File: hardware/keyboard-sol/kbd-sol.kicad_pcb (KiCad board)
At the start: 2 copper layers, 396.2 x 117.7 mm, 186 parts, among them J1 Controller, SW10 TAB: 1.25x, SW11 I, SW12 2, SW13 Zero, SW14 Q, SW15 O, SW16 3, SW17 Dash, SW18 W, SW19 P, SW20 4, SW21 Caret, SW22 E, SW23 AT, SW24 5, SW25 LT Bracket, SW26 R, SW27 Return: 1.5x, SW28 6, SW29 Backslash, SW30 T, SW31 Line Feed, SW32 7, SW33 RT Bracket, SW34 Y, SW35 Load, SW36 LT Ctrl, SW37 J, SW38 Upper Case: 1.5x, SW39 M, SW4 ESC: 1.75x, SW40 Shift Lock: 1.5x, SW41 K, SW42 LT Shift: 1.5x, SW43 Comma, SW44 A, SW45 L, SW46 Z, SW47 Period, SW48 S, SW49 Semicolon, SW5 8, SW50 X, SW51 Slash, SW52 D, SW53 Colon, SW54 C, SW55 RT Shift: 2x, SW56 F, SW57 DEL, SW58 V, SW59 Mode Select: 1.75x, SW6 BREAK, SW60 G, SW61 Repeat: 1.25x, SW62 B, SW63 H, SW64 RT Ctrl, SW65 N, SW66 Local, SW67 NP Dash, SW68 NP 4, SW69 NP Zero, SW7 U, SW70 Up Arrow, SW71 NP 7, SW72 NP 1, SW73 NP period, SW74 LT Arrow, SW75 NP asterisk, SW76 NP 5, SW77 NP plus, SW78 Spacebar, SW79 NP 8, SW8 1, SW80 NP 2, SW81 RT Arrow, SW82 NP divide, SW83 NP 6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

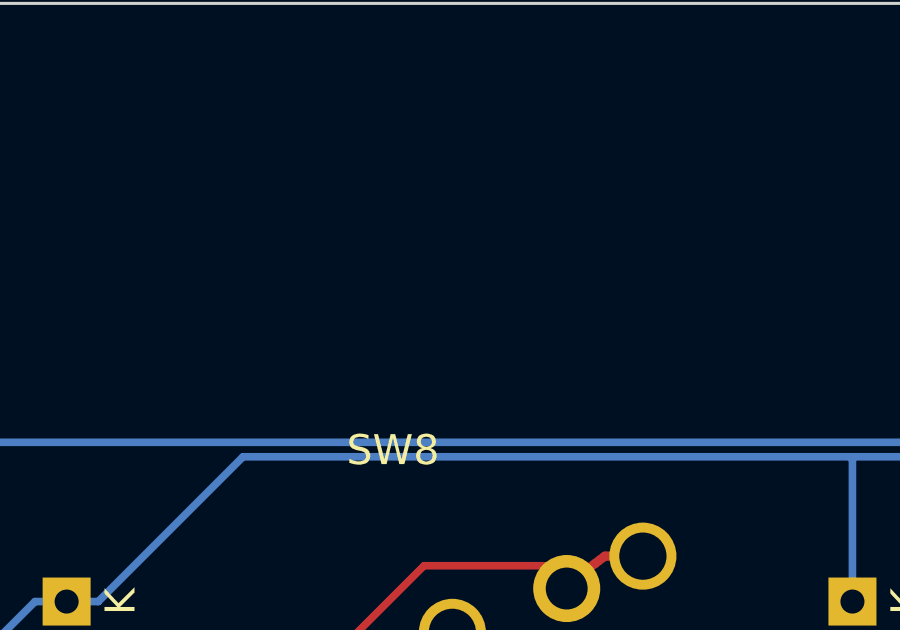
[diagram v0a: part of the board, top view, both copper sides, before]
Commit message: Add additional mounting holes to ASCII interface PCBS and Sol-20 PCB
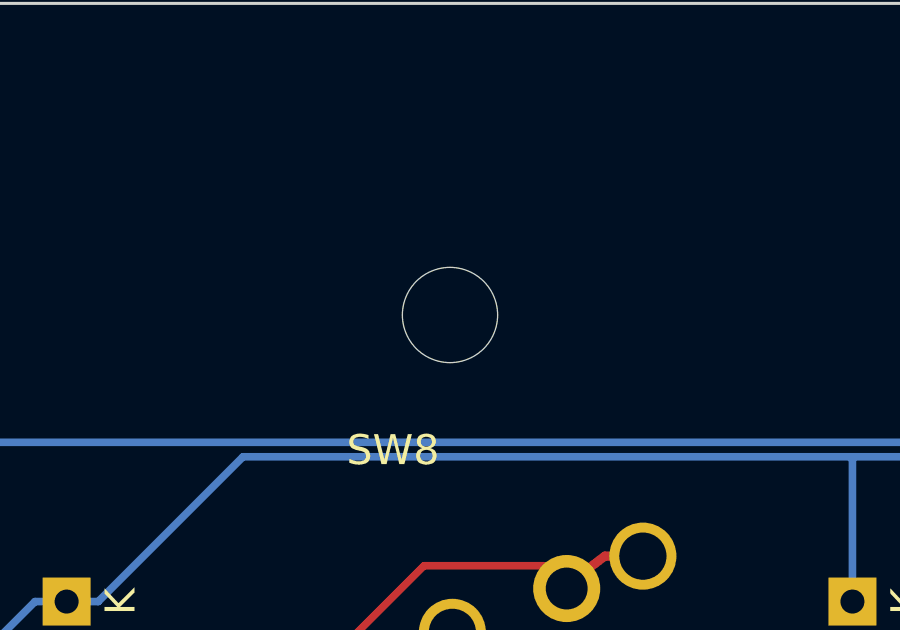
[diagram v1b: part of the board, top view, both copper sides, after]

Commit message: Add mounting holes for PCB along right side of keyboard
- moving interface PCB to right side eliminates clearance issues.
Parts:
- added REF**: MountingHole_3.2mm_M3, MountingHole:MountingHole_3.2mm_M3, F.Cu at (359.5, 114.1)
- added REF**: MountingHole_3.2mm_M3, MountingHole:MountingHole_3.2mm_M3, F.Cu at (392.7, 114.1)
- added REF**: MountingHole_3.2mm_M3, MountingHole:MountingHole_3.2mm_M3, F.Cu at (461.1, 114.1)
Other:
- board text added: "Interface MNT"
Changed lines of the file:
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@@
   (general
     (thickness 1.6)
-    (drawings 8)
+    (drawings 13)
     (tracks 1440)
     (zones 0)
-    (modules 186)
+    (modules 189)
     (nets 129)
   )
@@
     (add_net /Col0)
   )
+  (module MountingHole:MountingHole_3.2mm_M3 (layer F.Cu)
+    (at 359.5116 114.08156)
+    (descr "Mounting Hole 3.2mm, no annular, M3")
+    (tags "mounting hole 3.2mm no annular m3")
+    (attr virtual)
+    (fp_text reference REF** (at 0 -4.2) (layer F.SilkS) hide
+      (effects (font (size 1 1) (thickness 0.15)))
+    )
+    (fp_text value MountingHole_3.2mm_M3 (at 0 4.2) (layer F.Fab)
+      (effects (font (size 1 1) (thickness 0.15)))
+    )
+    (fp_circle (center 0 0) (end 3.45 0) (layer F.CrtYd) (width 0.05))
+    (fp_circle (center 0 0) (end 3.2 0) (layer Cmts.User) (width 0.15))
+    (fp_text user %R (at 0.3 0) (layer F.Fab)
+      (effects (font (size 1 1) (thickness 0.15)))
+    )
+    (pad 1 np_thru_hole circle (at 0 0) (size 3.2 3.2) (drill 3.2) (layers *.Cu *.Mask))
+  )
+  (module MountingHole:MountingHole_3.2mm_M3 (layer F.Cu)
+    (at 392.6586 114.08156)
+    (descr "Mounting Hole 3.2mm, no annular, M3")
+    (tags "mounting hole 3.2mm no annular m3")
+    (attr virtual)
+    (fp_text reference REF** (at 0 -4.2) (layer F.SilkS) hide
+      (effects (font (size 1 1) (thickness 0.15)))
+    )
+    (fp_text value MountingHole_3.2mm_M3 (at 0 4.2) (layer F.Fab)
+      (effects (font (size 1 1) (thickness 0.15)))
+    )
+    (fp_circle (center 0 0) (end 3.45 0) (layer F.CrtYd) (width 0.05))
+    (fp_circle (center 0 0) (end 3.2 0) (layer Cmts.User) (width 0.15))
+    (fp_text user %R (at 0.3 0) (layer F.Fab)
+      (effects (font (size 1 1) (thickness 0.15)))
+    )
+    (pad 1 np_thru_hole circle (at 0 0) (size 3.2 3.2) (drill 3.2) (layers *.Cu *.Mask))
+  )
+  (module MountingHole:MountingHole_3.2mm_M3 (layer F.Cu)
+    (at 461.1116 114.08156)
+    (descr "Mounting Hole 3.2mm, no annular, M3")
+    (tags "mounting hole 3.2mm no annular m3")
+    (attr virtual)
+    (fp_text reference REF** (at 0 -4.2) (layer F.SilkS) hide
+      (effects (font (size 1 1) (thickness 0.15)))
+    )
+    (fp_text value MountingHole_3.2mm_M3 (at 0 4.2) (layer F.Fab)
+      (effects (font (size 1 1) (thickness 0.15)))
+    )
+    (fp_text user %R (at 0.3 0) (layer F.Fab)
+      (effects (font (size 1 1) (thickness 0.15)))
+    )
+    (fp_circle (center 0 0) (end 3.2 0) (layer Cmts.User) (width 0.15))
+    (fp_circle (center 0 0) (end 3.45 0) (layer F.CrtYd) (width 0.05))
+    (pad 1 np_thru_hole circle (at 0 0) (size 3.2 3.2) (drill 3.2) (layers *.Cu *.Mask))
+  )
   (module unikbd:kbd_header_two_mounting_holes locked (layer F.Cu)
     (at 191.6938 208.9658 90)
@@
     )
   )
+  (gr_line (start 193.4464 117.2718) (end 237.6551 117.2718) (layer F.SilkS) (width 0.254))
+  (gr_text "Interface MNT" (at 214.8713 115.3541) (layer F.SilkS)
+    (effects (font (size 1.5 1.5) (thickness 0.3)))
+  )
+  (gr_text "Interface MNT" (at 459.7908 109.1565) (layer F.SilkS)
+    (effects (font (size 1.5 1.5) (thickness 0.3)))
+  )
+  (gr_line (start 363.2327 113.8174) (end 389.1407 113.8174) (layer F.SilkS) (width 0.254))
+  (gr_text "Interface MNT" (at 376.0343 112.3188) (layer F.SilkS)
+    (effects (font (size 1.5 1.5) (thickness 0.3)))
+  )
   (gr_text "SOL-20 keyboard rev 1.4" (at 362.7374 223.1644) (layer F.SilkS)

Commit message: Update Sol keyboard to 1.5 (Minor changes)
- Fix title in Schematic

- Slightly enlarge center post hole on switch footprint, to allow a bit of
tolerance. Very tight tolerance makes the keyboards hard to assemble.
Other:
- board text added: "SOL-20 keyboard rev 1.5"
- board text removed: "SOL-20 keyboard rev 1.4"

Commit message: Multiple fixes for keyboard PCB
- in combined CherryMX/futaba footprints, moved cherry pads down 1 mil and
futaba pads up 2 mil, to reduce risk of shortin of LED pads with futaba pad.
Adjusted all aligners accordingly

- Fixed centroid for combined diode footprint and adjusted PCB placement on
classic and SOL keyboards accordingly.

- Moved SMT pads in combined diode footprint to top layer, so pick & place file
will be usable.

- changes to futaba stabilizer design.  Longer post adapter passes through slots
in keyboard and aligner.

- Changed futaba post thickness gauge from board outline to a slot to improve
tolerance.

- Moved spacebar stabilizer bending guide to edge of PCB, in order to make it
more useful in bending PCBs.

- Changed Apple II mounting slots on classic keyboard from horizontal to
vertical orientation, to accommodate the different spacing offets due to the use
of spacers in angled mounting threads.
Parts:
- D1, D10, D11, D12, D13, D14, D15, D16, D17, D18, D19, D2, D20, D21, D22, D23, D24, D25, D26, D27, D28, D29, D3, D30, D31, D32, D33, D34, D35, D36, D37, D38, D39, D4, D40, D41, D42, D43, D44, D45, D46, D47, D48, D49, D5, D50, D51, D52, D53, D54, D55, D56, D57, D58, D59, D6, D60, D61, D62, D63, D64, D65, D66, D67, D68, D69, D7, D70, D71, D72, D73, D74, D75, D76, D77, D78, D79, D8, D80, D81, D82, D83, D84, D85, D9: footprint Diode_THT:D_DO-35_SOD27_P7.62mm_Horizontal -> unikbd:diode-combined
- moved D10 0.10 mm to (322.8, 127.0)
- moved D12 0.10 mm to (313.2, 146.1)
- moved D13 0.10 mm to (189.4, 127.0)
- moved D14 0.10 mm to (341.8, 127.0)
- moved D18 0.10 mm to (360.9, 127.0)
- moved D19 0.10 mm to (198.9, 146.1)
- moved D20 0.10 mm to (351.4, 146.1)
- moved D21 0.10 mm to (227.5, 127.0)
- moved D23 0.10 mm to (217.9, 146.1)
- moved D24 0.10 mm to (375.2, 146.1)
- moved D26 0.10 mm to (399.0, 127.0)
- moved D28 0.10 mm to (399.0, 146.1)
- moved D29 0.10 mm to (265.6, 127.0)
- moved D30 0.10 mm to (418.0, 127.0)
- moved D31 0.10 mm to (256.1, 146.1)
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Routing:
- net /Row1: track 346.6 -> 345.9 mm

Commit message: Update Sol-20 keyboard to use fixed footprints
- Update all footprints on sol-20 keyboard and aligners

- Add soldermask clearance around cherry MX posts

- Move Cherry MX pads down 1 mil, and Futaba pads up 2 mils

- Adjust Cherry aligner footprints down 1 mil

- Adjust Futaba aligner footprints up 2 mils

- Move mounting slots up 1 mil on Cherry aligner

- Move mounting slots down 1 mil on Futaba aligner

- incorporate improved stabilizer post adapters in futaba aligner

- add slots for stabilizer posts in futaba aligner and Sol kebyoard PCB

- Move stabilizer bar bend guide to left bottom edge to facilitate bending

- Bump rev to 1.6
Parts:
- D1, D10, D11, D12, D13, D14, D15, D16, D17, D18, D19, D2, D20, D21, D22, D23, D24, D25, D26, D27, D28, D29, D3, D30, D31, D32, D33, D34, D35, D36, D37, D38, D39, D4, D40, D41, D42, D43, D44, D45, D46, D47, D48, D49, D5, D50, D51, D52, D53, D54, D55, D56, D57, D58, D59, D6, D60, D61, D62, D63, D64, D65, D66, D67, D68, D69, D7, D70, D71, D72, D73, D74, D75, D76, D77, D78, D79, D8, D80, D81, D82, D83, D84, D85, D9: moved to B.Cu
- moved D1 3.53 mm to (125.1, 130.6)
- moved D10 3.53 mm to (322.8, 130.6)
- moved D13 3.53 mm to (189.4, 130.6)
- moved D14 3.53 mm to (341.8, 130.6)
- moved D17 3.53 mm to (208.5, 130.6)
- moved D18 3.53 mm to (360.9, 130.6)
- moved D2 3.53 mm to (284.7, 130.6)
- moved D21 3.53 mm to (227.5, 130.6)
- moved D22 3.53 mm to (379.9, 130.6)
- moved D25 3.53 mm to (246.6, 130.6)
- moved D26 3.53 mm to (399.0, 130.6)
- moved D29 3.53 mm to (265.6, 130.6)
- moved D30 3.53 mm to (418.0, 130.6)
- moved D5 3.53 mm to (151.3, 130.6)
- moved D6 3.53 mm to (303.7, 130.6)
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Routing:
- net /Col5: track 733.2 -> 743.8 mm
- net /Row2: track 238.7 -> 233.8 mm
- net /Row11: track 406.3 -> 409.2 mm
- net /Row12: track 274.5 -> 271.9 mm
- net /Row5: track 479.8 -> 477.2 mm
- net /Col1: track 809.7 -> 812.1 mm
- net /Col7: track 464.2 -> 463.1 mm
- net /Row10: track 443.7 -> 442.6 mm
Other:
- board text added: "SOL-20 keyboard rev 1.6"
- board text removed: "SOL-20 keyboard rev 1.5"

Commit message: Moved Cherry MX and futaba pads farther apart in combined footprint
- Offset cherry MX pads and aligners downward 0.004" from origin

- Offset futaba pads and aligners upward -0.004" from origin

- Update footprints in classic and sol-20 pcbs and aligners

- adjust mounting slots in Sol-20 aligners to match futaba or cherry offset
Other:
- board text added: "SOL-20 keyboard rev 1.7"
- board text removed: "SOL-20 keyboard rev 1.6"

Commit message: Add SMD diodes and resistors to SOL keyboard
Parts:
- added R4: 470, Resistor_SMD:R_0805_2012Metric, B.Cu at (95.9, 190.4)
- added R5: 470, Resistor_SMD:R_0805_2012Metric, B.Cu at (95.9, 205.6)
- added R6: 470, Resistor_SMD:R_0805_2012Metric, B.Cu at (95.9, 176.4)
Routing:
- net Net-(LED3-Pad1): track 41.8 -> 46.8 mm
- net Net-(J1-Pad16): track 118.8 -> 123.8 mm
- net Net-(LED1-Pad1): track 12.8 -> 17.3 mm
- net Net-(J1-Pad8): track 119.6 -> 123.9 mm
- net Net-(J1-Pad24): track 161.7 -> 165.5 mm
- net Net-(LED2-Pad1): track 12.7 -> 16.5 mm
